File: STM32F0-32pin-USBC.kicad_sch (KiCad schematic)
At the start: 18 parts, among them J1 Conn_ARM_JTAG_SWD_10, U1 STM32F042K6Tx, U4 MCP2221AxSL

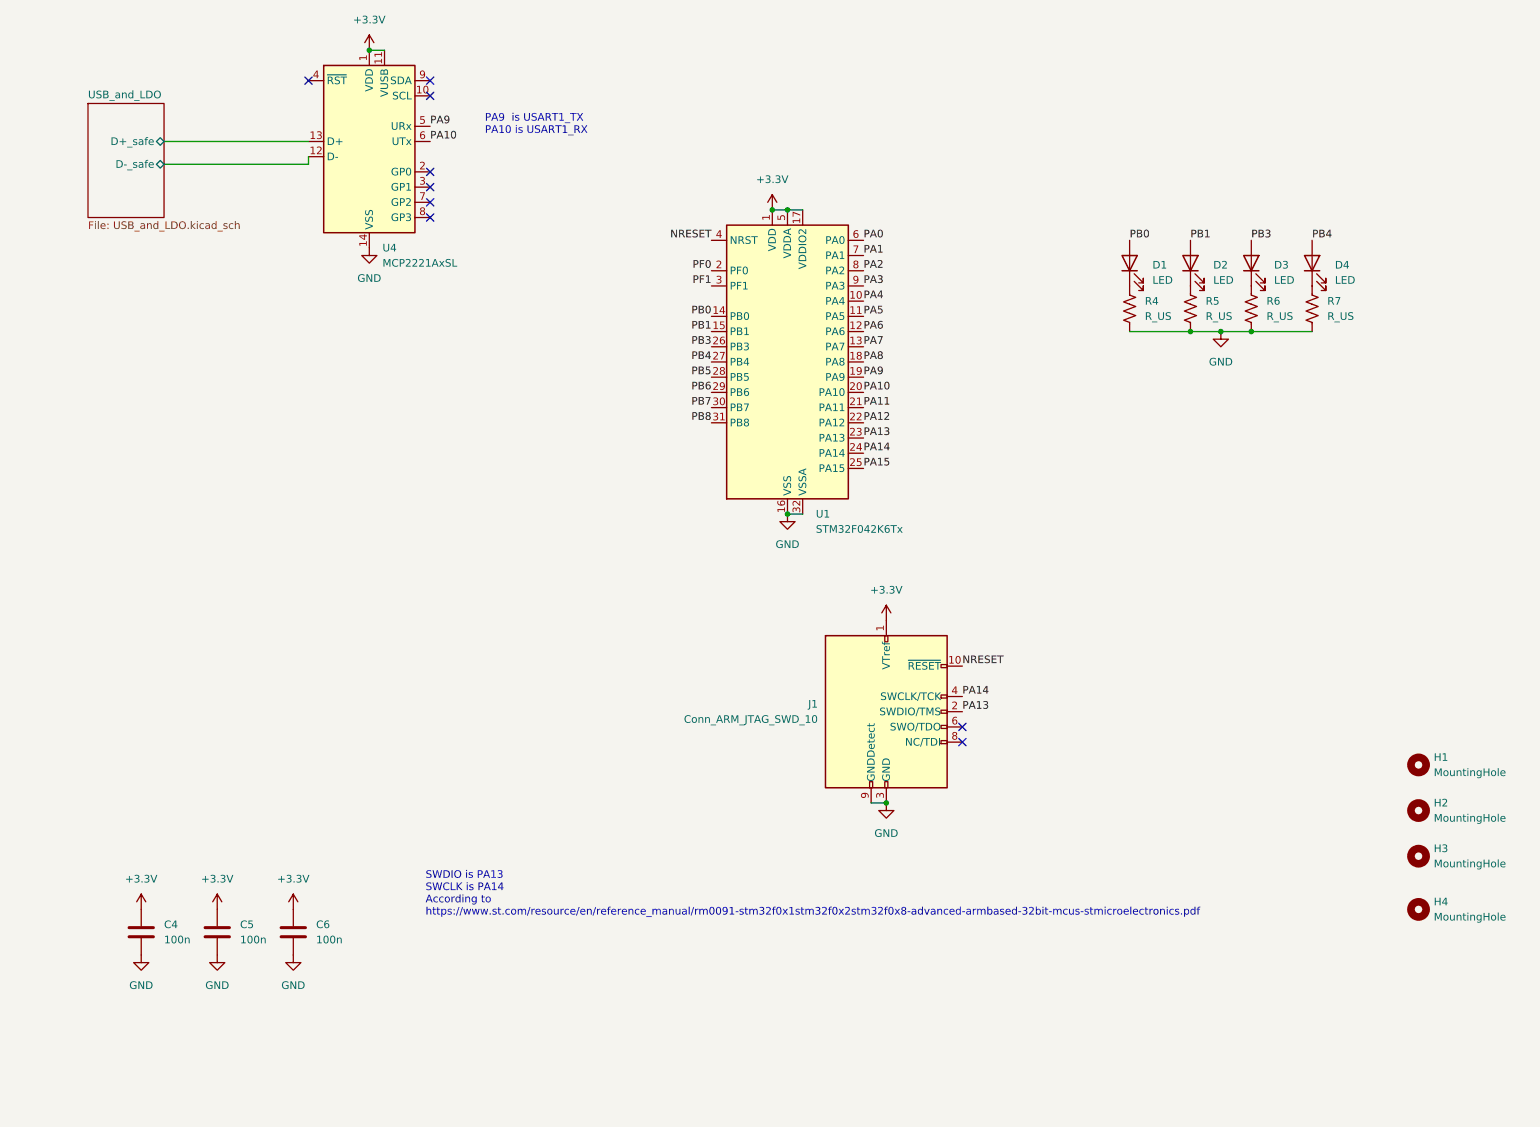
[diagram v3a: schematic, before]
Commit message: Finished schematic; ERC pass; still need footprints and part nums
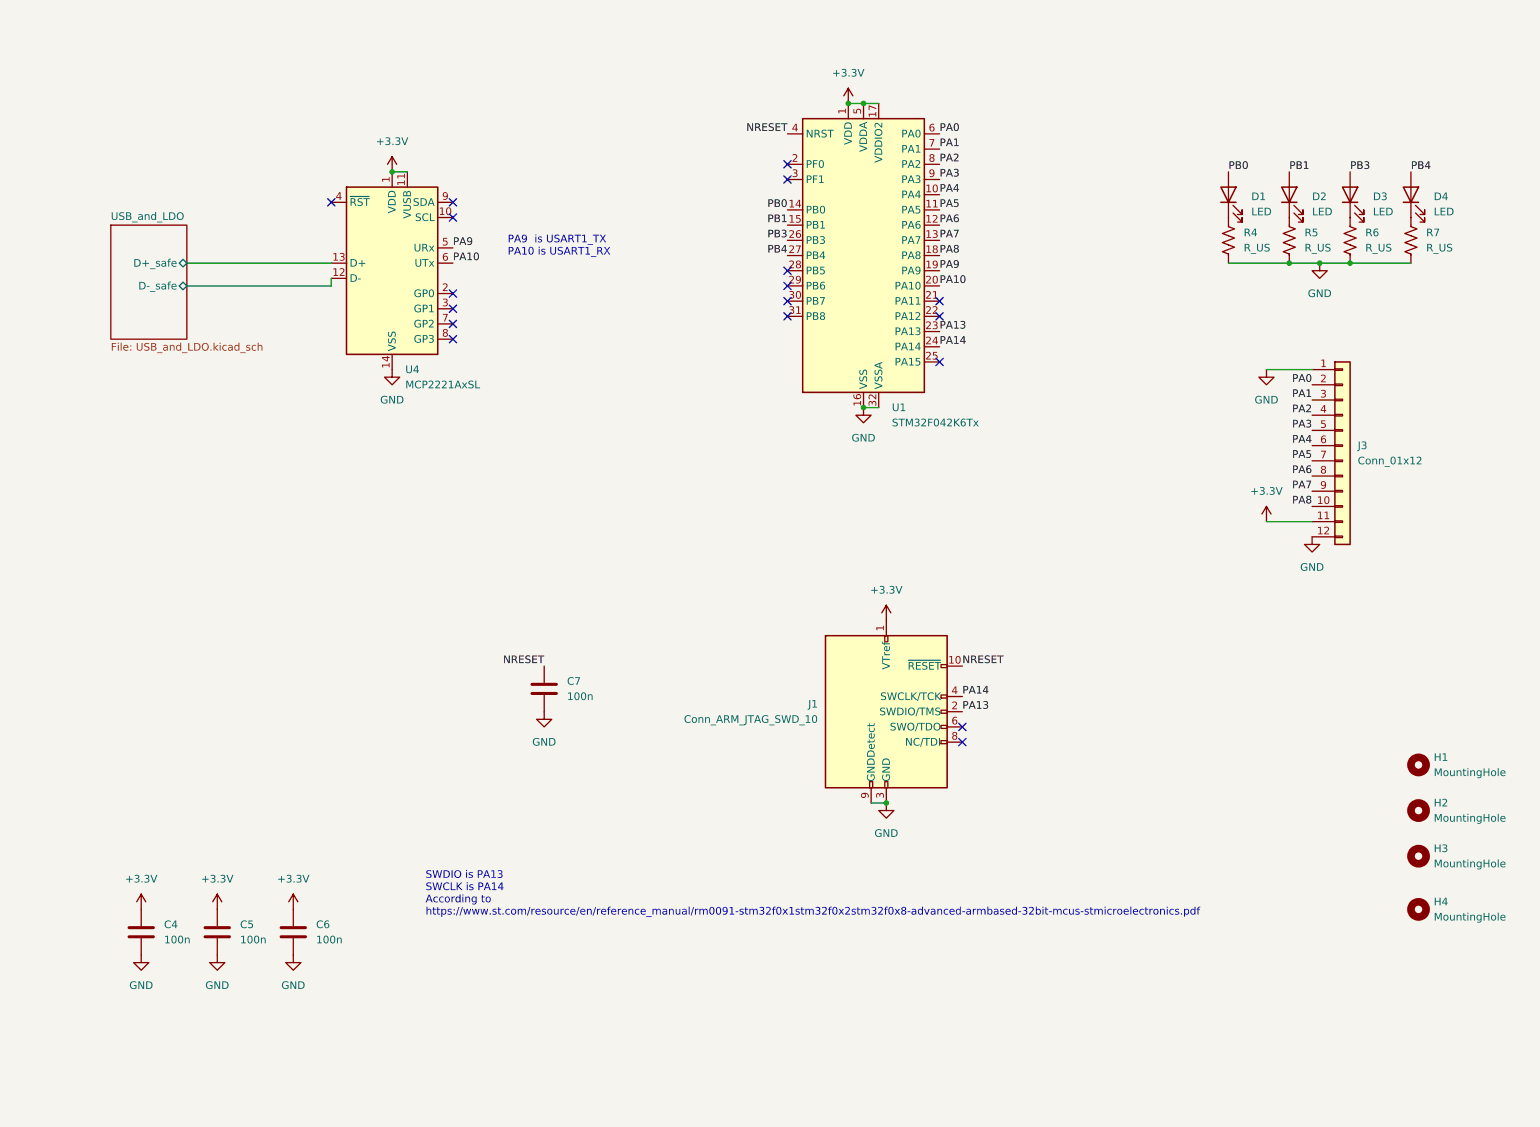
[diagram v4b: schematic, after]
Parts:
- added C7: 100n, symbol Device:C
- added J3: Conn_01x12, symbol Connector_Generic:Conn_01x12
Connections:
- net +3.3V: now also J3.11 (Pin_11)
- net GND: now also C7.2, J3.1 (Pin_1), J3.12 (Pin_12)
- net NRESET: now also C7.1
- net PA0: now also J3.2 (Pin_2)
- net PA1: now also J3.3 (Pin_3)
- net PA2: now also J3.4 (Pin_4)
- net PA3: now also J3.5 (Pin_5)
- net PA4: now also J3.6 (Pin_6)
- net PA5: now also J3.7 (Pin_7)
- net PA6: now also J3.8 (Pin_8)
- net PA7: now also J3.9 (Pin_9)
- net PA8: now also J3.10 (Pin_10)
- net PA11: no longer names the net of U1.21 (PA11)
- net PA12: no longer names the net of U1.22 (PA12)
- net PA15: no longer names the net of U1.25 (PA15)
- net PB5: no longer names the net of U1.28 (PB5)
- net PB6: no longer names the net of U1.29 (PB6)
- net PB7: no longer names the net of U1.30 (PB7)
- net PB8: no longer names the net of U1.31 (PB8)
- net PF0: no longer names the net of U1.2 (PF0)
- net PF1: no longer names the net of U1.3 (PF1)
- no-connect marks 9 -> 18
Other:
- moved on the sheet: D1, D2, D3, D4, R4, R5, R6, R7, U1, U4

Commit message: Added all footprints
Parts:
- C4, C5, C6, C7: footprint (none) -> Capacitor_SMD:C_1206_3216Metric_Pad1.33x1.80mm_HandSolder
- D1, D2, D3, D4: footprint (none) -> LED_SMD:LED_1206_3216Metric_Pad1.42x1.75mm_HandSolder
- H1, H2, H3, H4: footprint (none) -> MountingHole:MountingHole_3.2mm_M3
- J1: footprint (none) -> Connector_PinHeader_1.27mm:PinHeader_2x05_P1.27mm_Vertical
- J3: footprint (none) -> Connector_PinHeader_2.54mm:PinHeader_1x12_P2.54mm_Vertical
- R4, R5, R6, R7: footprint (none) -> Resistor_SMD:R_1206_3216Metric_Pad1.30x1.75mm_HandSolder
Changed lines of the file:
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@@
 			)
 		)
-		(property "Footprint" ""
+		(property "Footprint" "MountingHole:MountingHole_3.2mm_M3"
 			(at 247.65 156.21 0)
 			(effects
@@
 			)
 		)
-		(property "Footprint" ""
+		(property "Footprint" "Resistor_SMD:R_1206_3216Metric_Pad1.30x1.75mm_HandSolder"
 			(at 216.916 53.594 90)
 			(effects
@@
 			)
 		)
-		(property "Footprint" ""
+		(property "Footprint" "MountingHole:MountingHole_3.2mm_M3"
 			(at 247.65 165.1 0)
 			(effects
@@
 			)
 		)
-		(property "Footprint" ""
+		(property "Footprint" "Connector_PinHeader_2.54mm:PinHeader_1x12_P2.54mm_Vertical"
 			(at 234.95 87.63 0)
 			(effects
@@
 			)
 		)
-		(property "Footprint" ""
+		(property "Footprint" "Capacitor_SMD:C_1206_3216Metric_Pad1.33x1.80mm_HandSolder"
 			(at 60.6552 172.72 0)
 			(effects
@@
 			)
 		)
-		(property "Footprint" ""
+		(property "Footprint" "Resistor_SMD:R_1206_3216Metric_Pad1.30x1.75mm_HandSolder"
 			(at 227.076 53.594 90)
 			(effects
@@
 			)
 		)
-		(property "Footprint" ""
+		(property "Footprint" "MountingHole:MountingHole_3.2mm_M3"
 			(at 247.65 148.59 0)
 			(effects
@@
 			)
 		)
-		(property "Footprint" ""
+		(property "Footprint" "Capacitor_SMD:C_1206_3216Metric_Pad1.33x1.80mm_HandSolder"
 			(at 102.5652 132.08 0)
 			(effects
@@
 			)
 		)
-		(property "Footprint" ""
+		(property "Footprint" "Resistor_SMD:R_1206_3216Metric_Pad1.30x1.75mm_HandSolder"
 			(at 247.396 53.594 90)
 			(effects
@@
 			)
 		)
-		(property "Footprint" ""
+		(property "Footprint" "LED_SMD:LED_1206_3216Metric_Pad1.42x1.75mm_HandSolder"
 			(at 215.9 45.72 0)
 			(effects
@@
 			)
 		)
-		(property "Footprint" ""
+		(property "Footprint" "Capacitor_SMD:C_1206_3216Metric_Pad1.33x1.80mm_HandSolder"
 			(at 47.9552 172.72 0)
 			(effects
@@
 			)
 		)
-		(property "Footprint" ""
+		(property "Footprint" "Connector_PinHeader_1.27mm:PinHeader_2x05_P1.27mm_Vertical"
 			(at 158.75 132.08 0)
 			(effects
@@
 			)
 		)
-		(property "Footprint" ""
+		(property "Footprint" "Resistor_SMD:R_1206_3216Metric_Pad1.30x1.75mm_HandSolder"
 			(at 237.236 53.594 90)
 			(effects
@@
 			)
 		)
-		(property "Footprint" ""
+		(property "Footprint" "LED_SMD:LED_1206_3216Metric_Pad1.42x1.75mm_HandSolder"
 			(at 246.38 45.72 0)
 			(effects
@@
 			)
 		)
-		(property "Footprint" ""
+		(property "Footprint" "LED_SMD:LED_1206_3216Metric_Pad1.42x1.75mm_HandSolder"
 			(at 236.22 45.72 0)
 			(effects
@@
 			)
 		)
-		(property "Footprint" ""
+		(property "Footprint" "Capacitor_SMD:C_1206_3216Metric_Pad1.33x1.80mm_HandSolder"
 			(at 35.2552 172.72 0)
 			(effects
@@
 			)
 		)
-		(property "Footprint" ""
+		(property "Footprint" "LED_SMD:LED_1206_3216Metric_Pad1.42x1.75mm_HandSolder"
 			(at 226.06 45.72 0)
 			(effects
@@
 			)
 		)
-		(property "Footprint" ""
+		(property "Footprint" "MountingHole:MountingHole_3.2mm_M3"
 			(at 247.65 140.97 0)
 			(effects

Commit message: finished part nubers in BOM
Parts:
- C4, C5, C6, C7: MFR (none) -> Kemet; MFR Part No (none) -> C1206C104K4RACTU
- D1, D2, D3, D4: MFR (none) -> Lite-On; MFR Part No (none) -> LTST-C150KRKT
- H1, H2, H3, H4: value MountingHole -> M3
- J1: MFR (none) -> Samtec; MFR Part No (none) -> FTSH-105-01-L-D-007-K
- J3: MFR (none) -> TE Connectivity; MFR Part No (none) -> 9-146285-0
- R4, R5, R6, R7: value R_US -> 270R; MFR (none) -> Vishay; MFR Part No (none) -> CRCW1206270RFKEA
- U1: MFR (none) -> STMicroelectronics; MFR Part No (none) -> STM32F042K6T6
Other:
- note added: "LTST-C150KRKT Red LEDs V_f 2.0 V typ 2.4 V max For 5 mA current: 260 Ohm ~ 270 Ohm"

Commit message: preliminary footprint placement
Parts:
- removed H3, H4: M3, MountingHole:MountingHole_3.2mm_M3, symbol Mechanical:MountingHole
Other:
- moved on the sheet: H1, H2

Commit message: update all R's and all C's but 10u to 0805 from 1206
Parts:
- C4, C5, C6, C7: footprint Capacitor_SMD:C_1206_3216Metric_Pad1.33x1.80mm_HandSolder -> Capacitor_SMD:C_0805_2012Metric_Pad1.18x1.45mm_HandSolder; MFR Part No C1206C104K4RACTU -> C0805C104K4RACTU
- R4, R5, R6, R7: footprint Resistor_SMD:R_1206_3216Metric_Pad1.30x1.75mm_HandSolder -> Resistor_SMD:R_0805_2012Metric_Pad1.20x1.40mm_HandSolder; MFR Part No CRCW1206270RFKEA -> CRCW0805270RFKEA
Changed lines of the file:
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@@
 			)
 		)
-		(property "Footprint" "Resistor_SMD:R_1206_3216Metric_Pad1.30x1.75mm_HandSolder"
+		(property "Footprint" "Resistor_SMD:R_0805_2012Metric_Pad1.20x1.40mm_HandSolder"
 			(at 216.916 53.594 90)
 			(effects
@@
 			)
 		)
-		(property "MFR Part No" "CRCW1206270RFKEA"
+		(property "MFR Part No" "CRCW0805270RFKEA"
 			(at 215.9 53.34 0)
 			(effects
@@
 			)
 		)
-		(property "Footprint" "Capacitor_SMD:C_1206_3216Metric_Pad1.33x1.80mm_HandSolder"
+		(property "Footprint" "Capacitor_SMD:C_0805_2012Metric_Pad1.18x1.45mm_HandSolder"
 			(at 60.6552 172.72 0)
 			(effects
@@
 			)
 		)
-		(property "MFR Part No" "C1206C104K4RACTU"
+		(property "MFR Part No" "C0805C104K4RACTU"
 			(at 59.69 168.91 0)
 			(effects
@@
 			)
 		)
-		(property "Footprint" "Resistor_SMD:R_1206_3216Metric_Pad1.30x1.75mm_HandSolder"
+		(property "Footprint" "Resistor_SMD:R_0805_2012Metric_Pad1.20x1.40mm_HandSolder"
 			(at 227.076 53.594 90)
 			(effects
@@
 			)
 		)
-		(property "MFR Part No" "CRCW1206270RFKEA"
+		(property "MFR Part No" "CRCW0805270RFKEA"
 			(at 226.06 53.34 0)
 			(effects
@@
 			)
 		)
-		(property "Footprint" "Capacitor_SMD:C_1206_3216Metric_Pad1.33x1.80mm_HandSolder"
+		(property "Footprint" "Capacitor_SMD:C_0805_2012Metric_Pad1.18x1.45mm_HandSolder"
 			(at 102.5652 132.08 0)
 			(effects
@@
 			)
 		)
-		(property "MFR Part No" "C1206C104K4RACTU"
+		(property "MFR Part No" "C0805C104K4RACTU"
 			(at 101.6 128.27 0)
 			(effects
@@
 			)
 		)
-		(property "Footprint" "Resistor_SMD:R_1206_3216Metric_Pad1.30x1.75mm_HandSolder"
+		(property "Footprint" "Resistor_SMD:R_0805_2012Metric_Pad1.20x1.40mm_HandSolder"
 			(at 247.396 53.594 90)
 			(effects
@@
 			)
 		)
-		(property "MFR Part No" "CRCW1206270RFKEA"
+		(property "MFR Part No" "CRCW0805270RFKEA"
 			(at 246.38 53.34 0)
 			(effects
@@
 			)
 		)
-		(property "Footprint" "Capacitor_SMD:C_1206_3216Metric_Pad1.33x1.80mm_HandSolder"
+		(property "Footprint" "Capacitor_SMD:C_0805_2012Metric_Pad1.18x1.45mm_HandSolder"
 			(at 47.9552 172.72 0)
 			(effects
@@
 			)
 		)
-		(property "MFR Part No" "C1206C104K4RACTU"
+		(property "MFR Part No" "C0805C104K4RACTU"
 			(at 46.99 168.91 0)
 			(effects
@@
 			)
 		)
-		(property "Footprint" "Resistor_SMD:R_1206_3216Metric_Pad1.30x1.75mm_HandSolder"
+		(property "Footprint" "Resistor_SMD:R_0805_2012Metric_Pad1.20x1.40mm_HandSolder"
 			(at 237.236 53.594 90)
 			(effects
@@
 			)
 		)
-		(property "MFR Part No" "CRCW1206270RFKEA"
+		(property "MFR Part No" "CRCW0805270RFKEA"
 			(at 236.22 53.34 0)
 			(effects
@@
 			)
 		)
-		(property "Footprint" "Capacitor_SMD:C_1206_3216Metric_Pad1.33x1.80mm_HandSolder"
+		(property "Footprint" "Capacitor_SMD:C_0805_2012Metric_Pad1.18x1.45mm_HandSolder"
 			(at 35.2552 172.72 0)
 			(effects
@@
 			)
 		)
-		(property "MFR Part No" "C1206C104K4RACTU"
+		(property "MFR Part No" "C0805C104K4RACTU"
 			(at 34.29 168.91 0)
 			(effects
